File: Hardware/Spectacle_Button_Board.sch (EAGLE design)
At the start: 34 parts, among them J19 FTDI_DEVICE, U1 CY8C4146LQI-S422, U2 MIC5205-5V

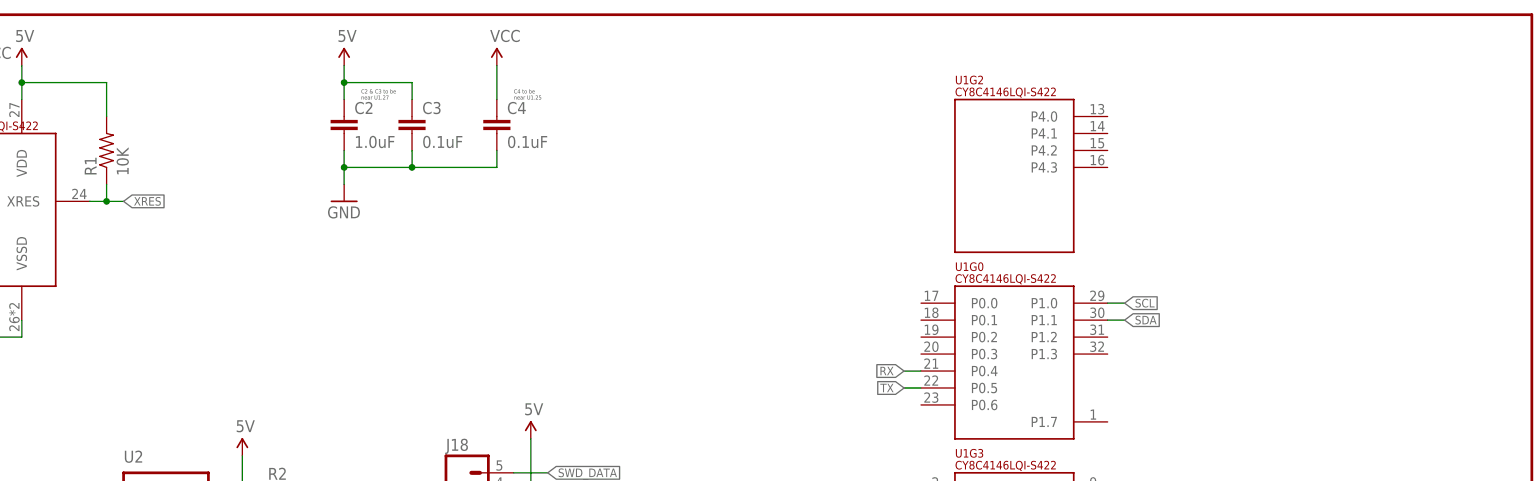
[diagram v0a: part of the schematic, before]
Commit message: Added LED, buttons
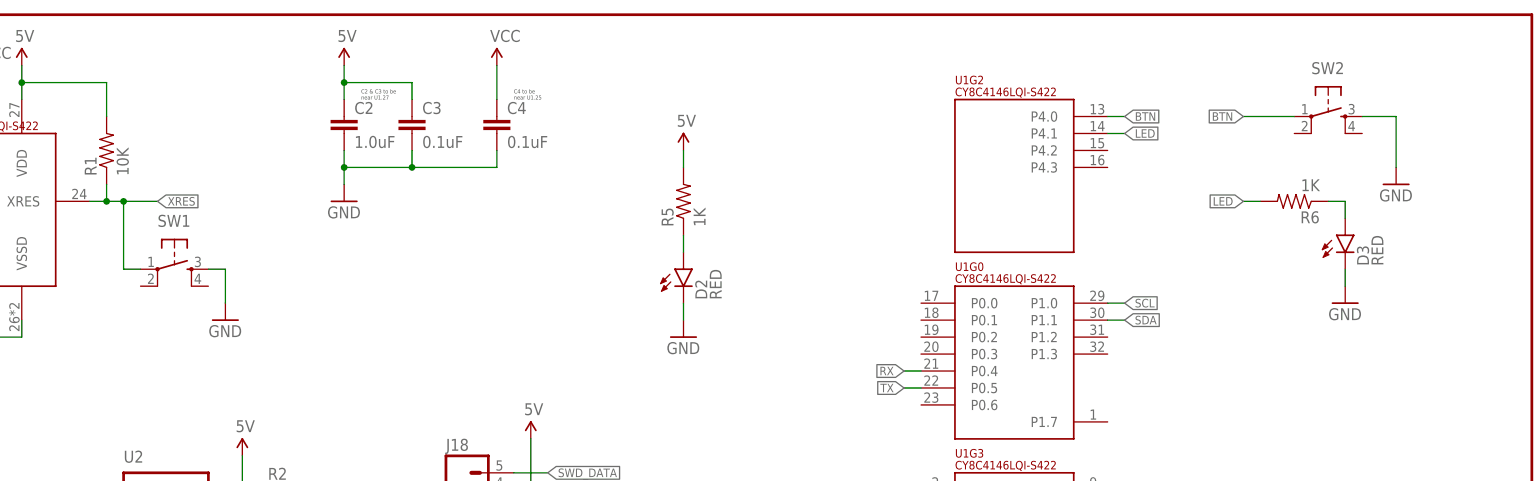
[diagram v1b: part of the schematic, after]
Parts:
- added D2, D3: RED, SparkFun-LED:LED-RED0603
- added R5, R6: 1K, SparkFun-Resistors:1KOHM-1/10W-1%(0603)
- added SW1, SW2: (no value), SparkFun-Electromechanical:SWITCH_SPST_4_PINRECT
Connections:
- new net BTN: SW2.1, U1G2.P4.0
- new net LED: R6.2, U1G2.P4.1
- new net N$4: D2.A, R5.1
- new net N$5: D3.A, R6.1
- net 5V: now also R5.2
- net GND: now also D2.C, D3.C, SW1.3, SW2.3
- net XRES: now also SW1.1
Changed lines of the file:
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@@
 <part name="SUPPLY10" library="SparkFun-Aesthetics" deviceset="VIN" device=""/>
 <part name="GND11" library="SparkFun-Aesthetics" deviceset="GND" device=""/>
+<part name="D2" library="SparkFun-LED" deviceset="LED-RED" device="0603" value="RED"/>
+<part name="SW1" library="SparkFun-Electromechanical" deviceset="SWITCH_SPST_4_PIN" device="RECT"/>
+<part name="SW2" library="SparkFun-Electromechanical" deviceset="SWITCH_SPST_4_PIN" device="RECT"/>
+<part name="D3" library="SparkFun-LED" deviceset="LED-RED" device="0603" value="RED"/>
+<part name="R5" library="SparkFun-Resistors" deviceset="1KOHM-1/10W-1%(0603)" device="" value="1K"/>
+<part name="GND12" library="SparkFun-Aesthetics" deviceset="GND" device=""/>
+<part name="GND13" library="SparkFun-Aesthetics" deviceset="GND" device=""/>
+<part name="GND14" library="SparkFun-Aesthetics" deviceset="GND" device=""/>
+<part name="R6" library="SparkFun-Resistors" deviceset="1KOHM-1/10W-1%(0603)" device="" value="1K"/>
+<part name="SUPPLY11" library="SparkFun-Aesthetics" deviceset="5V" device=""/>
+<part name="GND15" library="SparkFun-Aesthetics" deviceset="GND" device=""/>
 </parts>
 <sheets>
@@
 <instance part="SUPPLY10" gate="G$1" x="241.3" y="66.04"/>
 <instance part="GND11" gate="1" x="220.98" y="45.72"/>
+<instance part="D2" gate="G$1" x="121.92" y="147.32"/>
+<instance part="SW1" gate="G$1" x="45.72" y="147.32"/>
+<instance part="SW2" gate="G$1" x="218.44" y="170.18"/>
+<instance part="D3" gate="G$1" x="220.98" y="152.4"/>
+<instance part="R5" gate="G$1" x="121.92" y="157.48" rot="R90"/>
+<instance part="GND12" gate="1" x="121.92" y="137.16"/>
+<instance part="GND13" gate="1" x="220.98" y="142.24"/>
+<instance part="GND14" gate="1" x="228.6" y="160.02"/>
+<instance part="R6" gate="G$1" x="213.36" y="157.48" rot="R180"/>
+<instance part="SUPPLY11" gate="G$1" x="121.92" y="165.1"/>
+<instance part="GND15" gate="1" x="53.34" y="139.7"/>
 </instances>
 <busses>
@@
 <junction x="220.98" y="50.8"/>
 </segment>
+<segment>
+<pinref part="D3" gate="G$1" pin="C"/>
+<pinref part="GND13" gate="1" pin="GND"/>
+<wire x1="220.98" y1="147.32" x2="220.98" y2="144.78" width="0.1524" layer="91"/>
+</segment>
+<segment>
+<pinref part="SW2" gate="G$1" pin="3"/>
+<wire x1="223.52" y1="170.18" x2="228.6" y2="170.18" width="0.1524" layer="91"/>
+<wire x1="228.6" y1="170.18" x2="228.6" y2="162.56" width="0.1524" layer="91"/>
+<pinref part="GND14" gate="1" pin="GND"/>
+</segment>
+<segment>
+<pinref part="D2" gate="G$1" pin="C"/>
+<pinref part="GND12" gate="1" pin="GND"/>
+<wire x1="121.92" y1="142.24" x2="121.92" y2="139.7" width="0.1524" layer="91"/>
+</segment>
+<segment>
+<pinref part="SW1" gate="G$1" pin="3"/>
+<wire x1="50.8" y1="147.32" x2="53.34" y2="147.32" width="0.1524" layer="91"/>
+<pinref part="GND15" gate="1" pin="GND"/>
+<wire x1="53.34" y1="147.32" x2="53.34" y2="142.24" width="0.1524" layer="91"/>
+</segment>
 </net>
 <net name="IN_0" class="0">
@@
 <wire x1="99.06" y1="106.68" x2="96.52" y2="106.68" width="0.1524" layer="91"/>
 </segment>
+<segment>
+<pinref part="SUPPLY11" gate="G$1" pin="5V"/>
+<pinref part="R5" gate="G$1" pin="2"/>
+<wire x1="121.92" y1="165.1" x2="121.92" y2="162.56" width="0.1524" layer="91"/>
+</segment>
 </net>
 <net name="VCC" class="0">
@@
 <wire x1="35.56" y1="157.48" x2="38.1" y2="157.48" width="0.1524" layer="91"/>
 <junction x="35.56" y="157.48"/>
-<label x="38.1" y="157.48" size="1.27" layer="95" xref="yes"/>
+<label x="43.18" y="157.48" size="1.27" layer="95" xref="yes"/>
+<pinref part="SW1" gate="G$1" pin="1"/>
+<wire x1="38.1" y1="157.48" x2="43.18" y2="157.48" width="0.1524" layer="91"/>
+<wire x1="40.64" y1="147.32" x2="38.1" y2="147.32" width="0.1524" layer="91"/>
+<wire x1="38.1" y1="147.32" x2="38.1" y2="157.48" width="0.1524" layer="91"/>
+<junction x="38.1" y="157.48"/>
 </segment>
 <segment>
@@
 </segment>
 </net>
+<net name="N$4" class="0">
+<segment>
+<pinref part="D2" gate="G$1" pin="A"/>
+<pinref part="R5" gate="G$1" pin="1"/>
+<wire x1="121.92" y1="149.86" x2="121.92" y2="152.4" width="0.1524" layer="91"/>
+</segment>
+</net>
+<net name="BTN" class="0">
+<segment>
+<pinref part="U1" gate="G2" pin="P4.0"/>
+<wire x1="185.42" y1="170.18" x2="187.96" y2="170.18" width="0.1524" layer="91"/>
+<label x="187.96" y="170.18" size="1.27" layer="95" xref="yes"/>
+</segment>
+<segment>
+<pinref part="SW2" gate="G$1" pin="1"/>
+<wire x1="205.74" y1="170.18" x2="213.36" y2="170.18" width="0.1524" layer="91"/>
+<label x="205.74" y="170.18" size="1.27" layer="95" rot="R180" xref="yes"/>
+</segment>
+</net>
+<net name="LED" class="0">
+<segment>
+<pinref part="U1" gate="G2" pin="P4.1"/>
+<wire x1="185.42" y1="167.64" x2="187.96" y2="167.64" width="0.1524" layer="91"/>
+<label x="187.96" y="167.64" size="1.27" layer="95" xref="yes"/>
+</segment>
+<segment>
+<pinref part="R6" gate="G$1" pin="2"/>
+<wire x1="208.28" y1="157.48" x2="205.74" y2="157.48" width="0.1524" layer="91"/>
+<label x="205.74" y="157.48" size="1.27" layer="95" rot="R180" xref="yes"/>
+</segment>
+</net>
+<net name="N$5" class="0">
+<segment>
+<pinref part="R6" gate="G$1" pin="1"/>
+<pinref part="D3" gate="G$1" pin="A"/>
+<wire x1="218.44" y1="157.48" x2="220.98" y2="157.48" width="0.1524" layer="91"/>
+<wire x1="220.98" y1="157.48" x2="220.98" y2="154.94" width="0.1524" layer="91"/>
+</segment>
+</net>
